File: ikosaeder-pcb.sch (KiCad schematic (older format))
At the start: 5 parts, among them J1 Conn_01x03_Female, J2 Conn_01x03_Female, J3 Conn_01x03_Female, J4 Conn_01x03_Female, J5 Conn_01x03_Female

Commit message: Make the first pcb board which has the label A
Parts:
- added Power1: Conn_01x02_Female, Connector_PinHeader_2.54mm:PinHeader_1x02_P2.54mm_Vertical, symbol Connector:Conn_01x02_Female
- added Signal1: Conn_01x01_Female, Connector_PinHeader_2.54mm:PinHeader_1x01_P2.54mm_Vertical, symbol Connector:Conn_01x01_Female
- renumbered J4 to <C-34, J5 to <D-30, J3 to >B-35, J1 to >E-1, J2 to >F-31
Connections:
- net +5V: now also Power1.1 (Pin_1)
- net GND: now also >B-35.3 (Pin_3), Power1.2 (Pin_2)
- net at >E-1.2 (Pin_2): now also Signal1.1 (Pin_1)
- net at >F-31.2 (Pin_2): now also <D-30.2 (Pin_2)
- net at >B-35.2 (Pin_2): now also <C-34.2 (Pin_2)
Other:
- note added: "A"
- moved on the sheet: <C-34, <D-30, >B-35, >E-1, >F-31

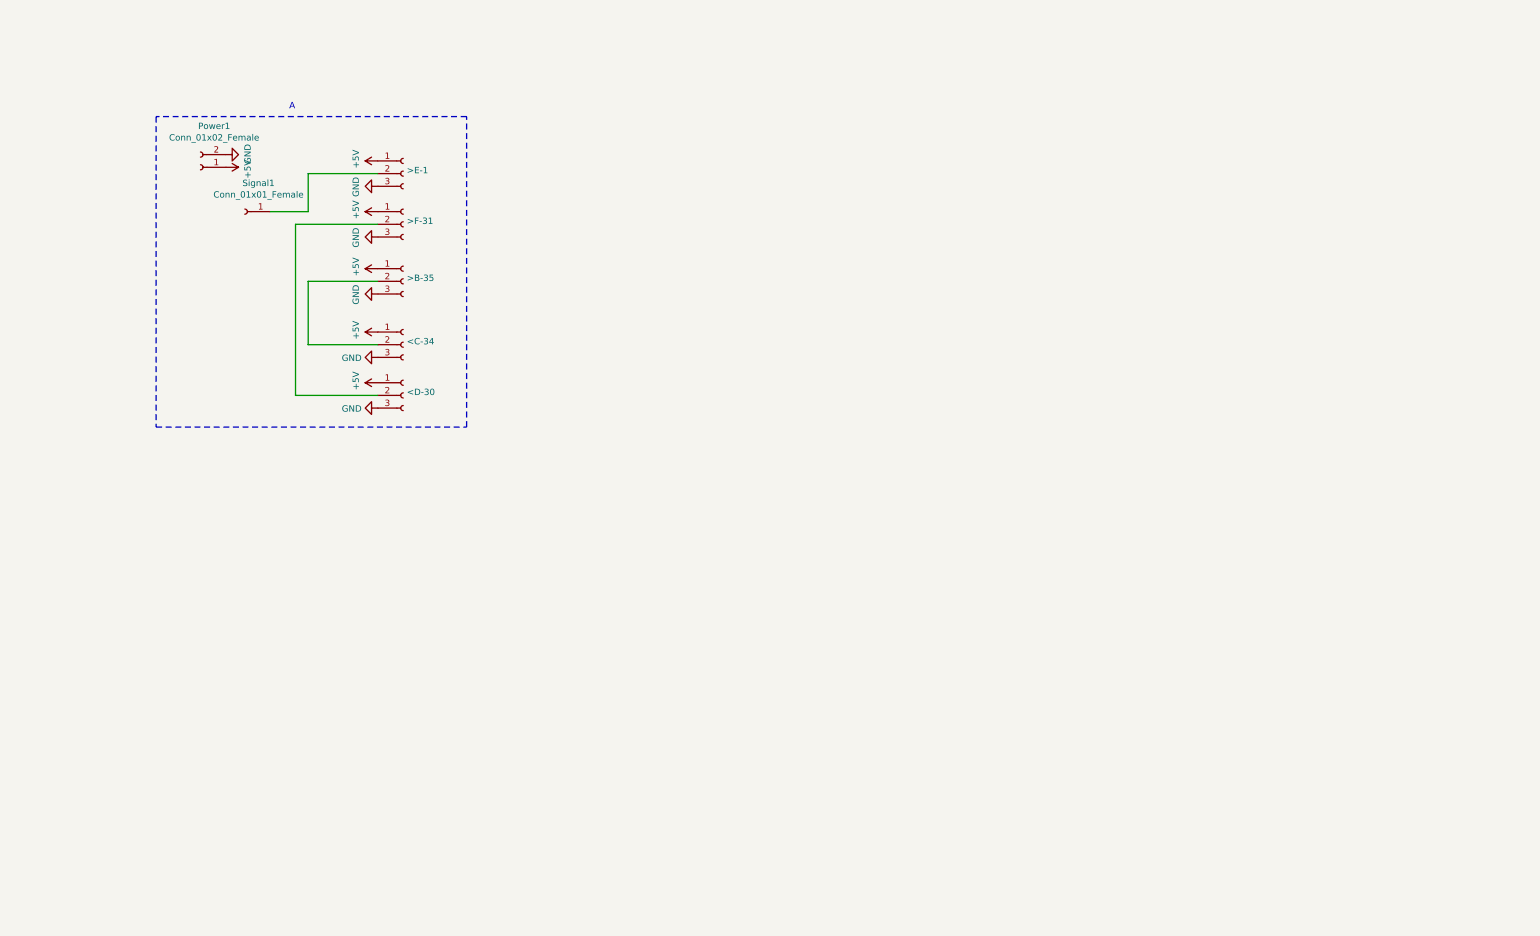
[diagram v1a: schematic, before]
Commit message: Minor tweaks
- Add male / female connector for semantic purposes
- Consolidate the connectors
- Prepare for 12 pcbs
- Use clockwise arrangement
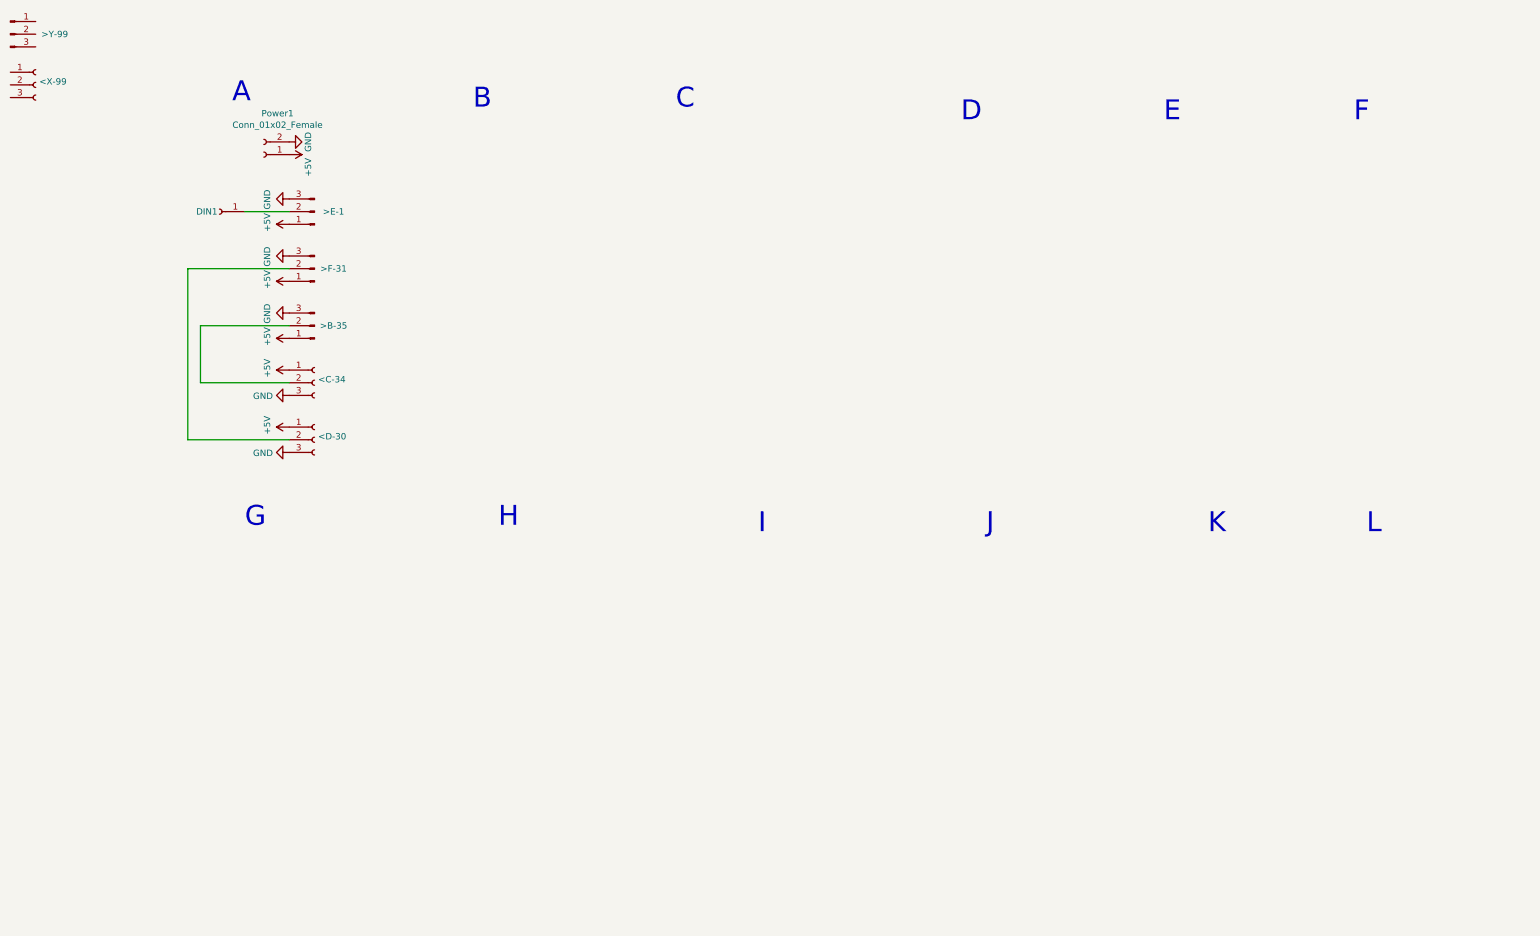
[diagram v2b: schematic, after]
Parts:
- removed >B-35, >E-1, >F-31: Conn_01x03_Female, Connector_PinSocket_2.54mm:PinSocket_1x03_P2.54mm_Vertical, symbol Connector:Conn_01x03_Female
- added <X-99: Conn_01x03_Female, Connector_PinSocket_2.54mm:PinSocket_1x03_P2.54mm_Vertical, symbol Connector:Conn_01x03_Female
- added >B-35, >E-1, >F-31, >Y-99: Conn_01x03_Male, Connector_PinHeader_2.54mm:PinHeader_1x03_P2.54mm_Vertical, symbol Connector:Conn_01x03_Male
- renumbered Signal1 to DIN1
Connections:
- net +5V: now also >B-35.1 (Pin_1), >E-1.1 (Pin_1), >F-31.1 (Pin_1)
- net GND: now also >B-35.3 (Pin_3), >E-1.3 (Pin_3), >F-31.3 (Pin_3)
- net at DIN1.1 (Pin_1): now also >E-1.2 (Pin_2)
- net at <D-30.2 (Pin_2): now also >F-31.2 (Pin_2)
- net at <C-34.2 (Pin_2): now also >B-35.2 (Pin_2)
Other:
- note added: "B"
- note added: "C"
- note added: "D"
- note added: "E"
- note added: "F"
- note added: "G"
- note added: "H"
- note added: "I"
- note added: "J"
- note added: "K"
- note added: "L"
- moved on the sheet: <C-34, <D-30, DIN1, Power1

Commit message: Ikosaeder final
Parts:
- removed <C-34, <D-30, <X-99: Conn_01x03_Female, Connector_PinSocket_2.54mm:PinSocket_1x03_P2.54mm_Vertical, symbol Connector:Conn_01x03_Female
- removed >B-35, >E-1, >F-31, >Y-99: Conn_01x03_Male, Connector_PinHeader_2.54mm:PinHeader_1x03_P2.54mm_Vertical, symbol Connector:Conn_01x03_Male
- added <=C.21, <=D.13, <=E.15, <=F.25, <=G.9: Conn_01x01_Female, Connector_PinHeader_2.54mm:PinHeader_1x01_P2.54mm_Vertical, symbol Connector:Conn_01x01_Female
- added <A.1, <A.31, <A.35, <B.27, <B.33, <C.29, <C.34, <D.23, <D.30, <E.2, <E.24, <F.17, <F.32, <G.19, <G.28, <H.11, <H.20, <H.22, <I.12, <I.14, <I.7, <J.16, <J.3, <J.6, <K.18, <K.26, <K.5, <L.10, <L.4, <L.8: LEDs_In, IkosaederFootprints:LED-Strip, symbol Ikosaeder:LEDs_In
- added =>H.21, =>I.13, =>J.15, =>K.25, =>L.9: Conn_01x01_Male, Connector_PinHeader_2.54mm:PinHeader_1x01_P2.54mm_Vertical, symbol Connector:Conn_01x01_Male
- added >A.30, >A.34, >B.26, >B.32, >B.35, >C.20, >C.28, >C.33, >D.12, >D.22, >D.29, >E.1, >E.14, >E.23, >F.16, >F.24, >F.31, >G.18, >G.27, >G.8, >H.10, >H.19, >I.11, >I.6, >J.2, >J.5, >K.17, >K.4, >L.3, >L.7: LEDs_Out, IkosaederFootprints:LED-Strip, symbol Ikosaeder:LEDs_Out
- added JP1: SolderJumper_2_Bridged, Jumper:SolderJumper-2_P1.3mm_Bridged_RoundedPad1.0x1.5mm, symbol Jumper:SolderJumper_2_Bridged
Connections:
- wire segments 7 -> 88
- no-connect marks 0 -> 1
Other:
- moved on the sheet: DIN1, Power1
